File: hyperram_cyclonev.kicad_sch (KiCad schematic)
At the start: 57 parts, among them IC1 AP63205WU, IC2 TXB0108PWR, IC3 S26KL128SDABHI020, IC4 W25Q32JVSSIQ_TR, IC5 S27KL0641DABHI020, J1 ASP-122952-01, J2 HDMI_A, J3 1156915, J4 1156915, J5 Conn_02x06_Top_Bottom, J6 Conn_02x06_Top_Bottom, J7 Conn_02x06_Top_Bottom, Q1 BSS138, Q2 BSS138

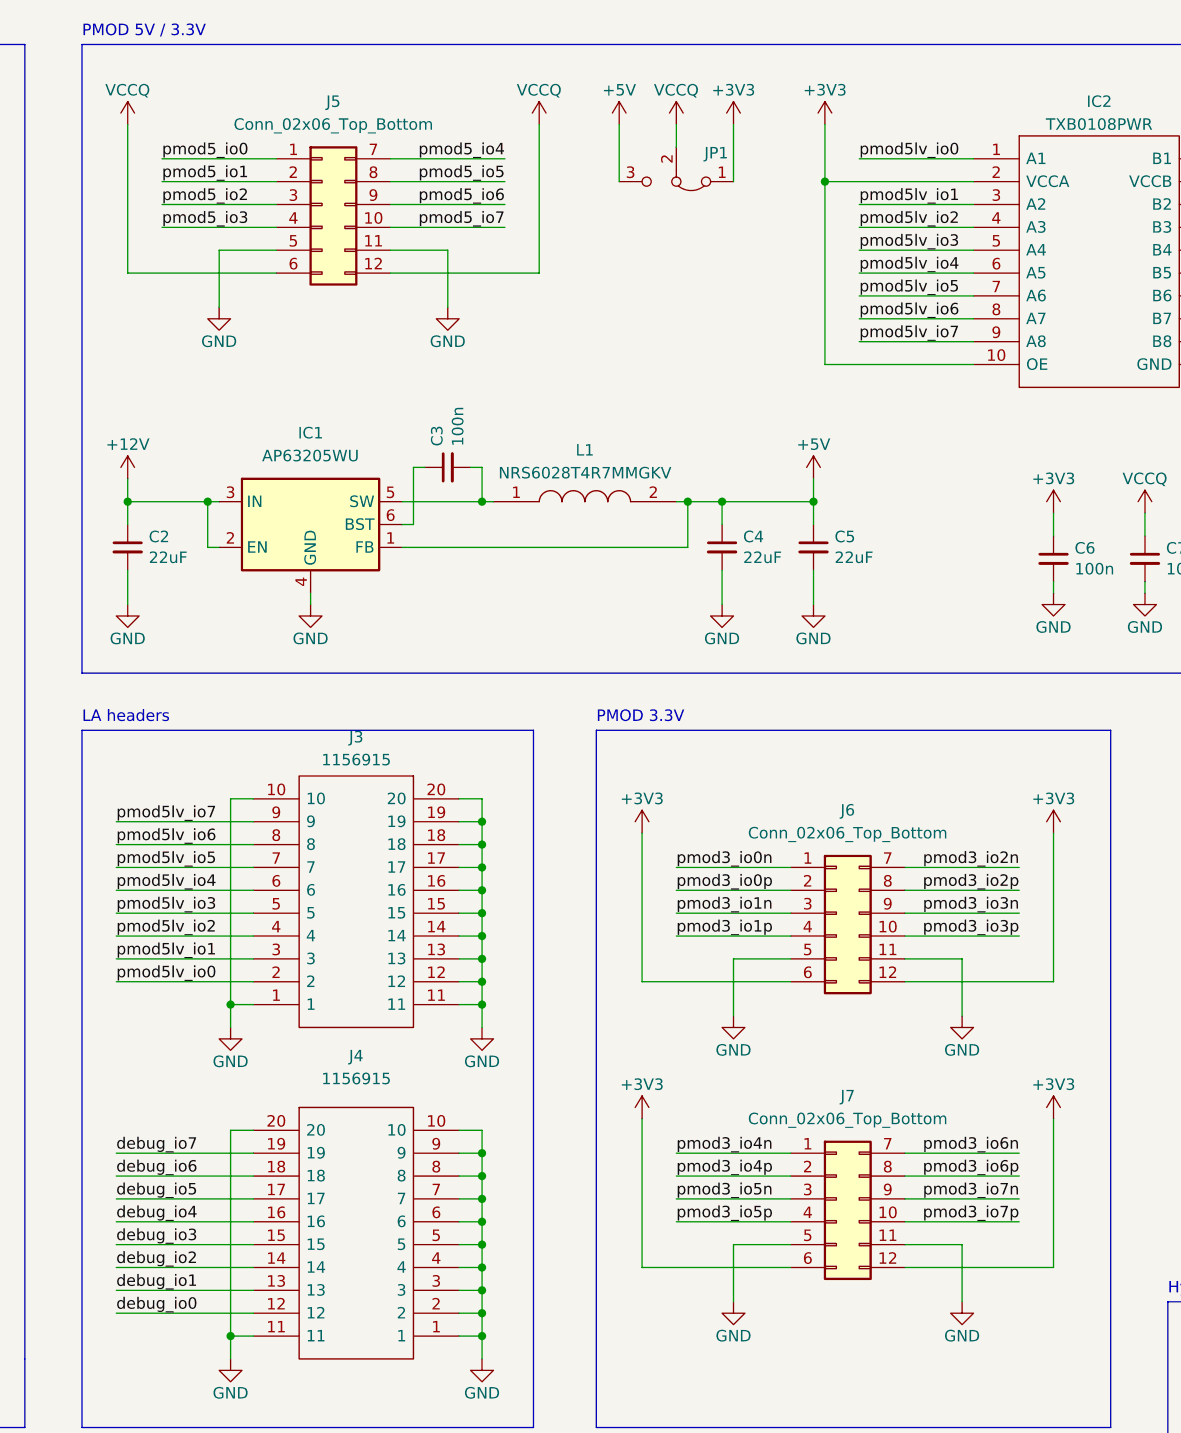
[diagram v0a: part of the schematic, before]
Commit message: Fixed issue with PMOD pins assignment
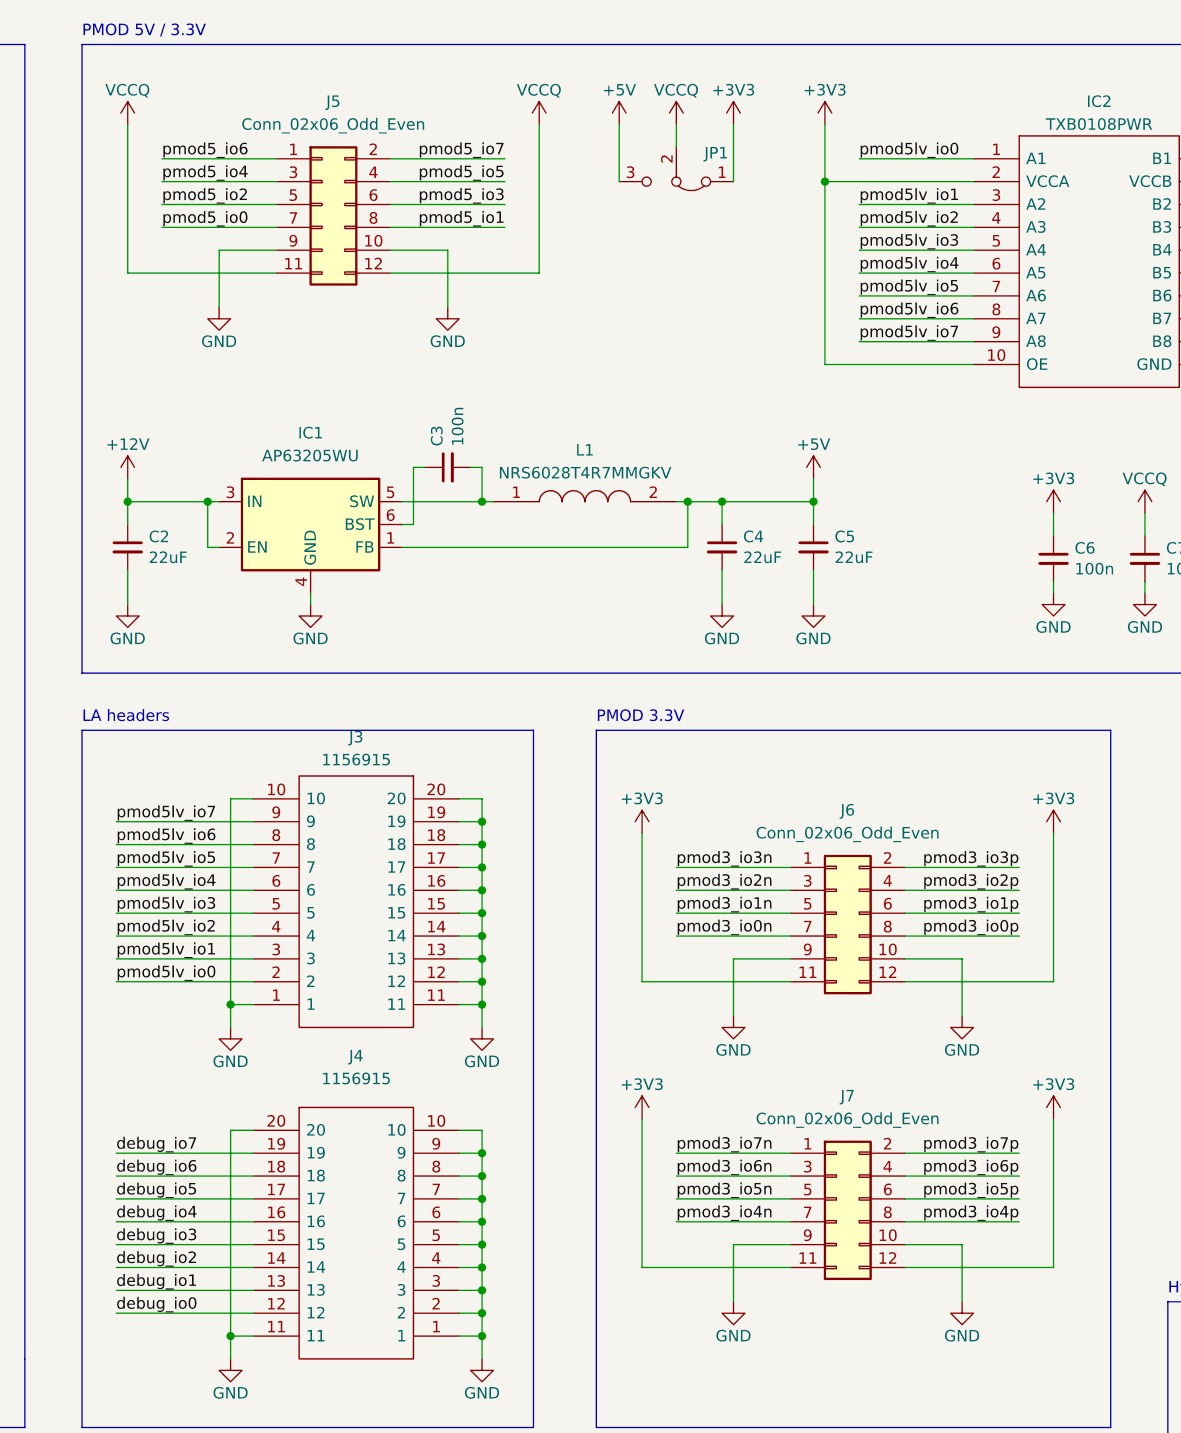
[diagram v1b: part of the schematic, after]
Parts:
- removed J5, J6, J7: Conn_02x06_Top_Bottom, hyperram_cyclonev:610112249221, symbol Connector_Generic:Conn_02x06_Top_Bottom
- added J5, J6, J7: Conn_02x06_Odd_Even, hyperram_cyclonev:610112249221, symbol Connector_Generic:Conn_02x06_Odd_Even
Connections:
- net +3V3: now also J6.11 (Pin_11), J6.12 (Pin_12), J7.11 (Pin_11), J7.12 (Pin_12)
- net GND: now also J5.10 (Pin_10), J5.9 (Pin_9), J6.10 (Pin_10), J6.9 (Pin_9), J7.10 (Pin_10), J7.9 (Pin_9)
- net VCCQ: now also J5.11 (Pin_11), J5.12 (Pin_12)
- net pmod3_io0n: now also J6.7 (Pin_7)
- net pmod3_io0p: now also J6.8 (Pin_8)
- net pmod3_io1n: now also J6.5 (Pin_5)
- net pmod3_io1p: now also J6.6 (Pin_6)
- net pmod3_io2n: now also J6.3 (Pin_3)
- net pmod3_io2p: now also J6.4 (Pin_4)
- net pmod3_io3n: now also J6.1 (Pin_1)
- net pmod3_io3p: now also J6.2 (Pin_2)
- net pmod3_io4n: now also J7.7 (Pin_7)
- net pmod3_io4p: now also J7.8 (Pin_8)
- net pmod3_io5n: now also J7.5 (Pin_5)
- net pmod3_io5p: now also J7.6 (Pin_6)
- net pmod3_io6n: now also J7.3 (Pin_3)
- net pmod3_io6p: now also J7.4 (Pin_4)
- net pmod3_io7n: now also J7.1 (Pin_1)
- net pmod3_io7p: now also J7.2 (Pin_2)
- net pmod5_io0: now also J5.7 (Pin_7)
- net pmod5_io1: now also J5.8 (Pin_8)
- net pmod5_io2: now also J5.5 (Pin_5)
- net pmod5_io3: now also J5.6 (Pin_6)
- net pmod5_io4: now also J5.3 (Pin_3)
- net pmod5_io5: now also J5.4 (Pin_4)
- net pmod5_io6: now also J5.1 (Pin_1)
- net pmod5_io7: now also J5.2 (Pin_2)

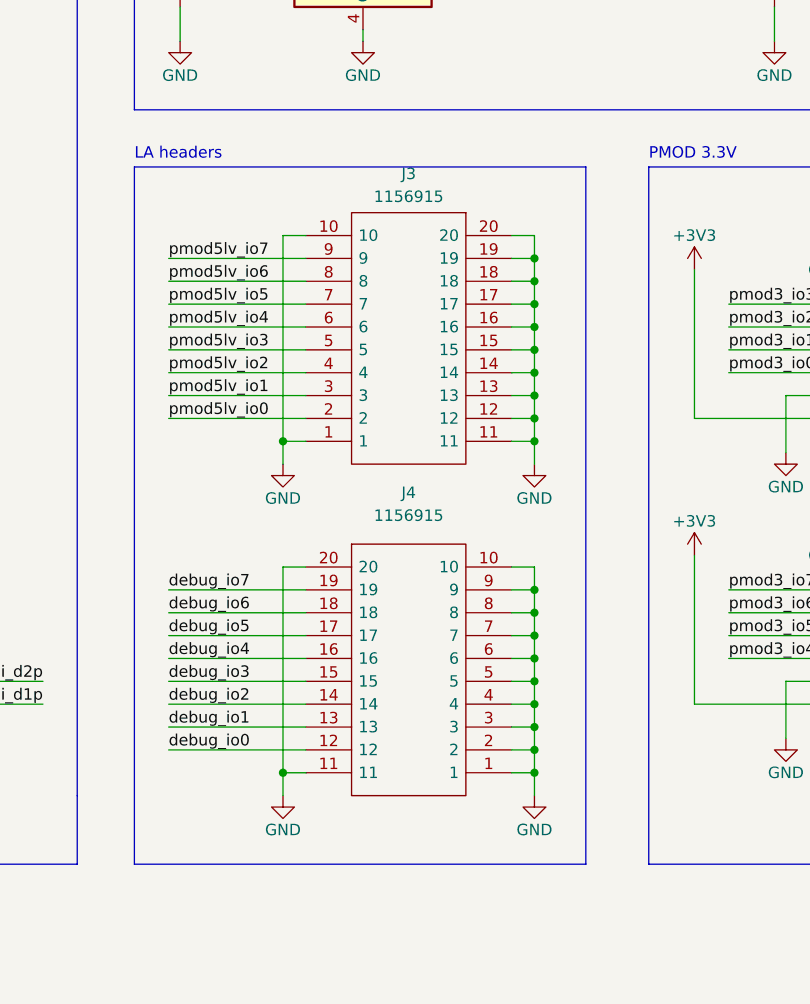
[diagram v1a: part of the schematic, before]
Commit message: Changed two connectors from SMD to THT
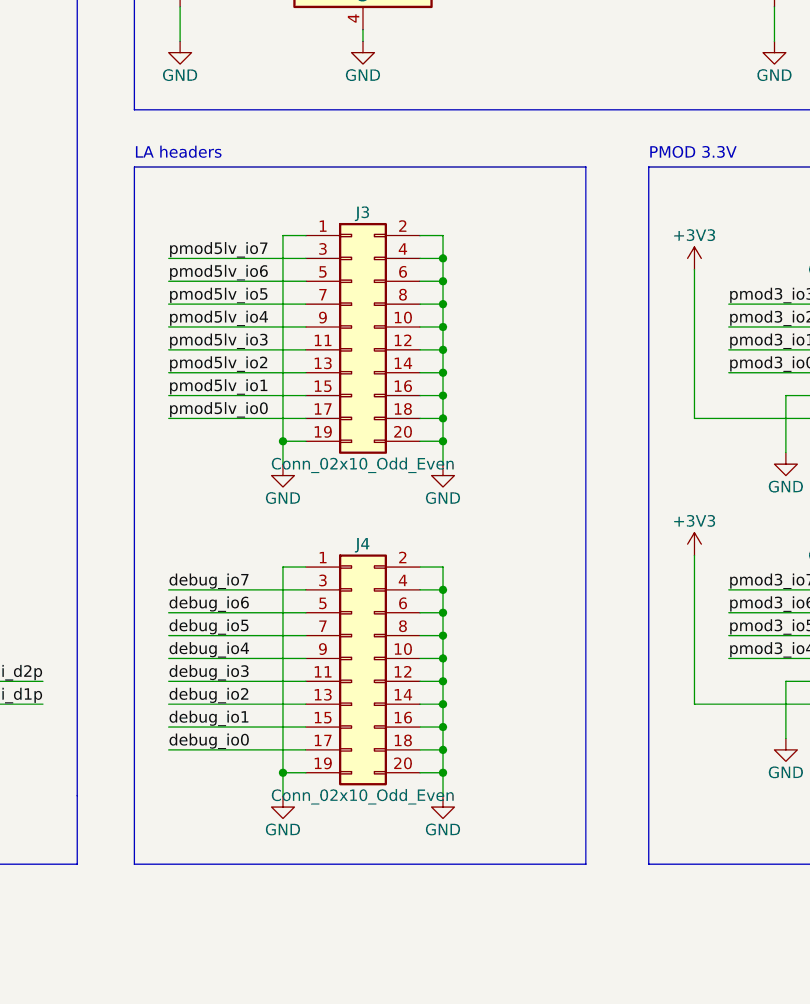
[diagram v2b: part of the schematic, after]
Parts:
- removed J3, J4: 1156915, hyperram_cyclonev:1156915, symbol hyperram_cyclonev:1156915
- added J3, J4: Conn_02x10_Odd_Even, Connector_PinHeader_2.54mm:PinHeader_2x10_P2.54mm_Vertical, symbol Connector_Generic:Conn_02x10_Odd_Even
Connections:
- net GND: now also J3.1 (Pin_1), J3.10 (Pin_10), J3.12 (Pin_12), J3.14 (Pin_14), J3.16 (Pin_16), J3.18 (Pin_18), J3.19 (Pin_19), J3.2 (Pin_2), J3.20 (Pin_20), J3.4 (Pin_4), J3.6 (Pin_6), J3.8 (Pin_8), J4.1 (Pin_1), J4.10 (Pin_10), J4.12 (Pin_12), J4.14 (Pin_14), J4.16 (Pin_16), J4.18 (Pin_18), J4.19 (Pin_19), J4.2 (Pin_2), J4.20 (Pin_20), J4.4 (Pin_4), J4.6 (Pin_6), J4.8 (Pin_8)
- net debug_io0: now also J4.17 (Pin_17)
- net debug_io1: now also J4.15 (Pin_15)
- net debug_io2: now also J4.13 (Pin_13)
- net debug_io3: now also J4.11 (Pin_11)
- net debug_io4: now also J4.9 (Pin_9)
- net debug_io5: now also J4.7 (Pin_7)
- net debug_io6: now also J4.5 (Pin_5)
- net debug_io7: now also J4.3 (Pin_3)
- net pmod5lv_io0: now also J3.17 (Pin_17)
- net pmod5lv_io1: now also J3.15 (Pin_15)
- net pmod5lv_io2: now also J3.13 (Pin_13)
- net pmod5lv_io3: now also J3.11 (Pin_11)
- net pmod5lv_io4: now also J3.9 (Pin_9)
- net pmod5lv_io5: now also J3.7 (Pin_7)
- net pmod5lv_io6: now also J3.5 (Pin_5)
- net pmod5lv_io7: now also J3.3 (Pin_3)
